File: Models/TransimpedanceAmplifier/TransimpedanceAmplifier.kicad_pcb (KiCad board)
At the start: 2 copper layers, 107 parts, among them J1 Conn_01x02_Socket, J10 Conn_01x02_Pin, J11 Conn_01x24_Socket, J14 Conn_01x24_Socket, J2 Conn_01x02_Socket, J3 Conn_01x03_Pin, J4 Conn_01x02_Pin, J5 Conn_01x02_Pin, J6 Conn_01x02_Pin, J7 Conn_01x02_Pin, J8 Conn_01x02_Pin, J9 Conn_01x02_Pin, Q1 Q_PNP, Q2 Q_NPN, U1 LM7905, -5V, 5%, U10 DAC81401, U11 ISO7641FM, U12 ISO7641FM, U13 ADS8699, U2 LM7805, 5V, 5%, U3 OPA828, U4 AD8615, U5 OP37GPZ, U6 LM7915, -15V, 5%, U7 LM7815, 15V, 5%, U8 LM7805, 5V, 5%, U9 TLV76133, 3.3V, 1%

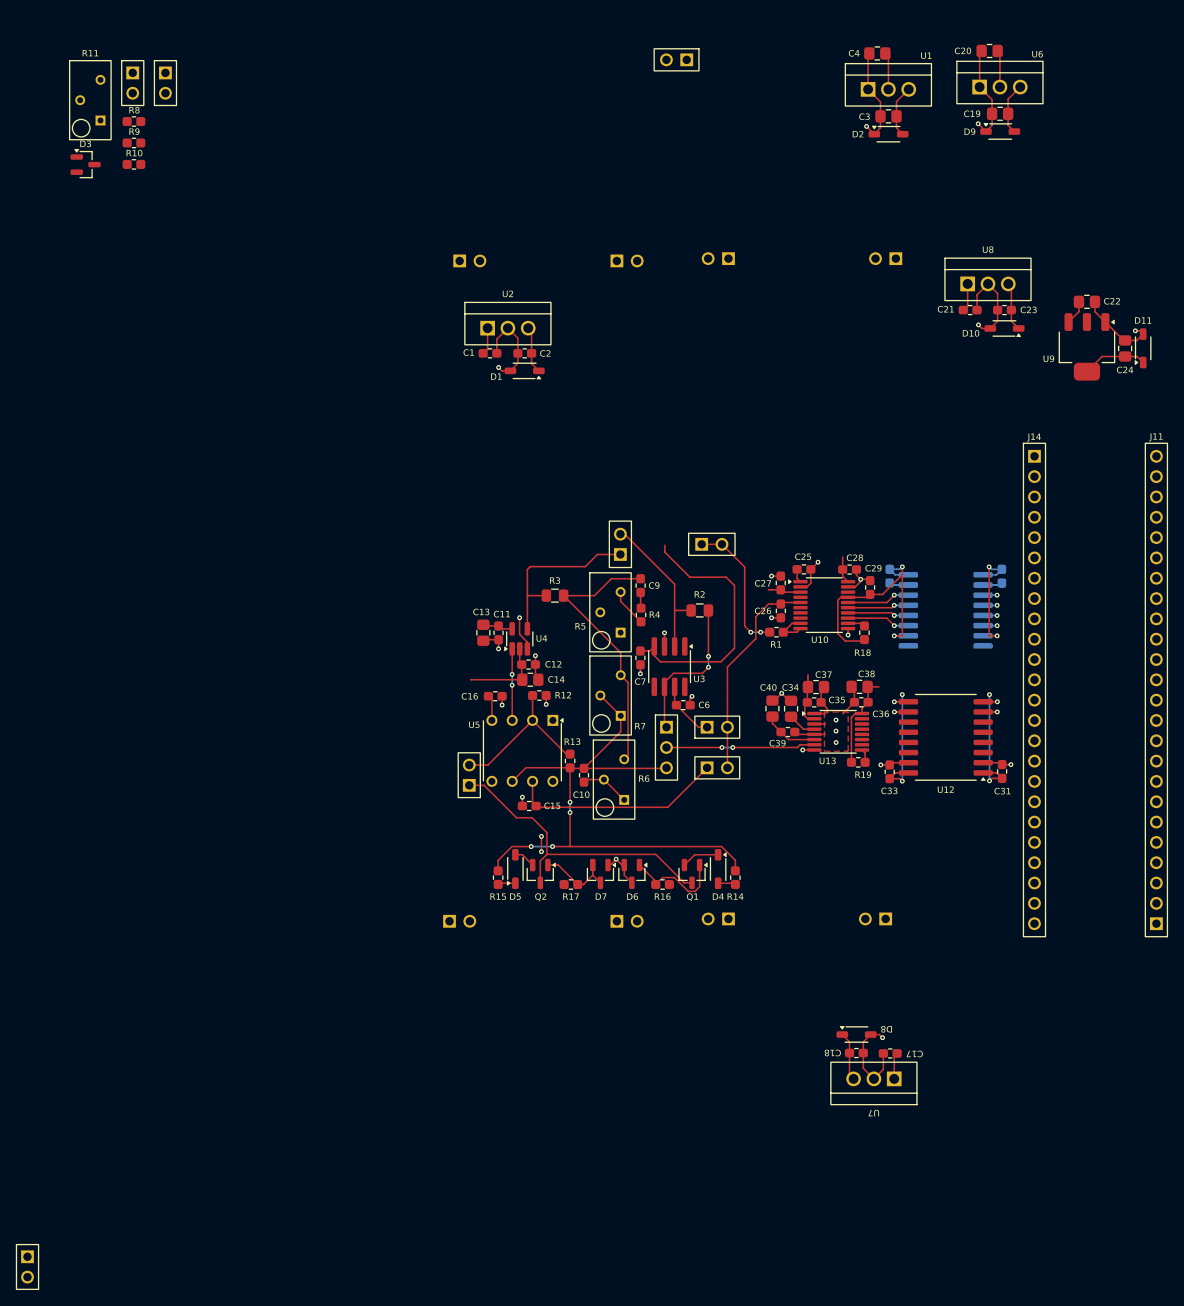
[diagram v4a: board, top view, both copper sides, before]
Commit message: Finalized the positions of all expensive chips and their nearby components
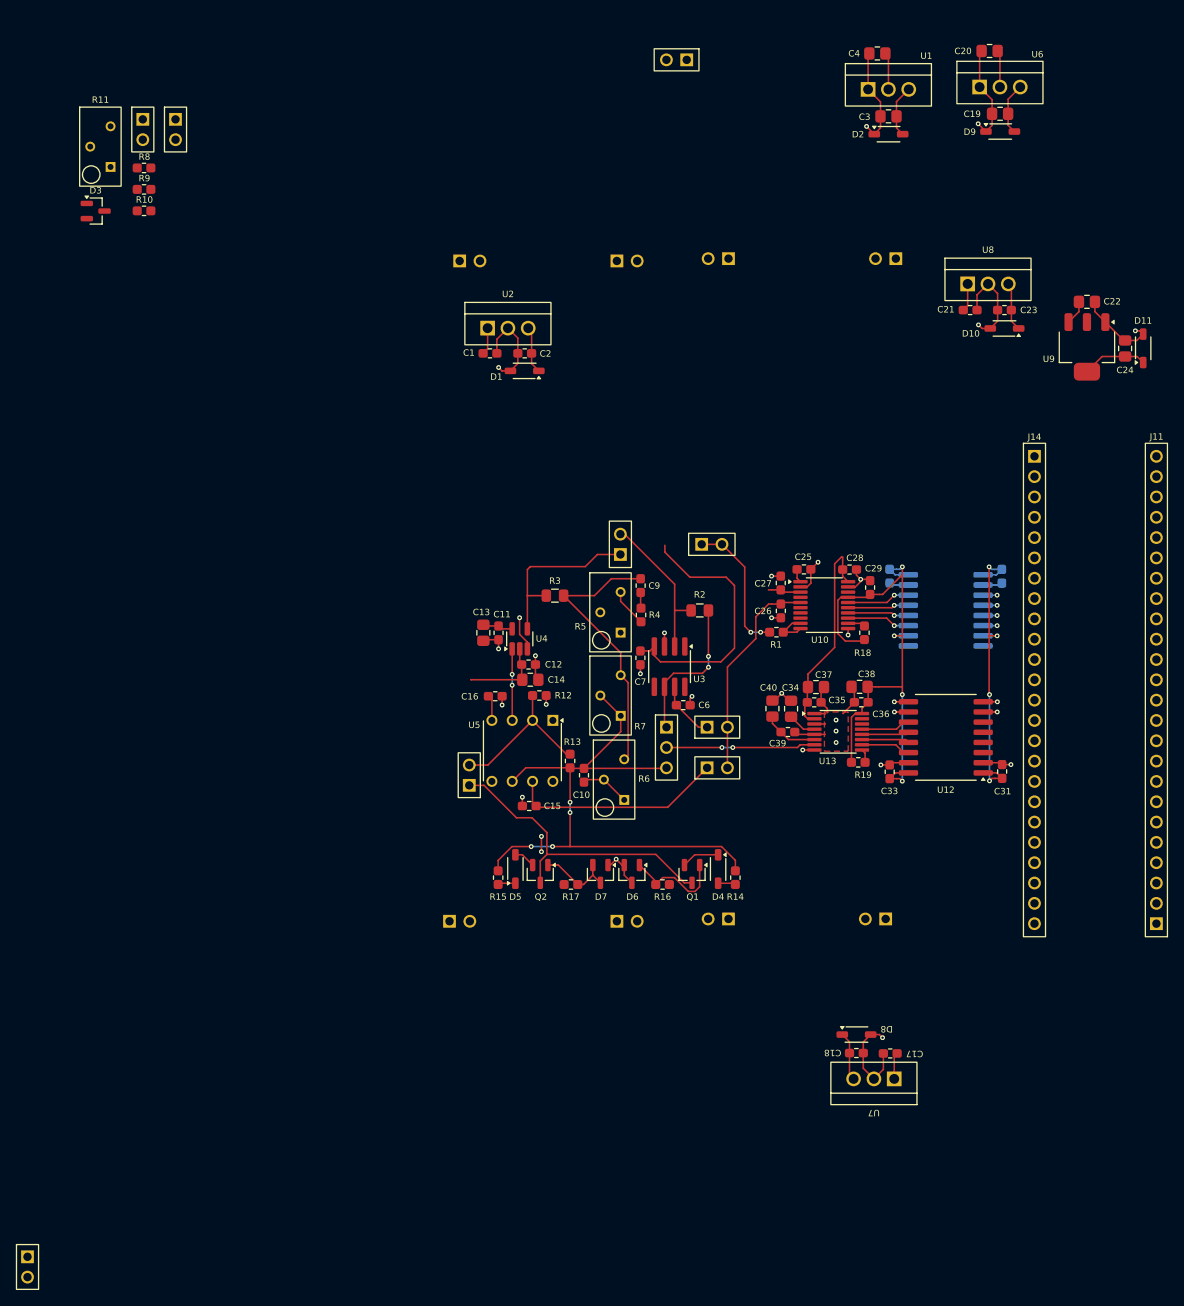
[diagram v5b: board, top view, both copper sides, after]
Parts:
- moved J6 5.94 mm to (37.8, 33.8)
- moved J7 5.94 mm to (41.9, 33.8)
- moved R11 5.94 mm to (32.5, 36.0)
- moved D3 5.94 mm to (31.9, 44.0)
- moved R10 5.94 mm to (38.0, 44.0)
- moved R8 5.94 mm to (38.0, 38.6)
- moved R9 5.94 mm to (38.0, 41.3)
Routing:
- net /5V_Converter: track 9.17 -> 25.8 mm
- net /3.3V_Converter: track 37.5 -> 47.7 mm
- net /CPU/Isolation/3.3V_Digital: track 25.8 -> 33.1 mm
- net /CPU/ADC/MOSI: track 0.00 -> 6.21 mm
- net /CPU/ADC/MISO: track 0.00 -> 6.17 mm
- net /CPU/ADC/CS: track 0.00 -> 5.95 mm
- net /CPU/ADC/SCK: track 0.00 -> 5.92 mm
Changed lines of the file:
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@@
 	(footprint "Connector_Custom:PinHeader_1x2"
 		(layer "F.Cu")
-		(at 40.6325 28.005)
+		(at 41.89 33.81)
 		(property "Reference" "J7"
 			(at 0.0025 -3.5625 0)
@@
 	)
 	(footprint "TwoTerminal:RESC0603"
+		(locked yes)
 		(layer "F.Cu")
 		(at 117.005 96.645 180)
@@
 	)
 	(footprint "TwoTerminal:CAPC0603"
+		(locked yes)
 		(layer "F.Cu")
 		(at 121.7275 105.415)
@@
 	(footprint "Connector_Custom:PinHeader_1x2"
 		(layer "F.Cu")
-		(at 36.5425 28.005)
+		(at 37.8 33.81)
 		(property "Reference" "J6"
 			(at 0.0025 -3.5625 0)
@@
 	)
 	(footprint "TwoTerminal:CAPC0805"
+		(locked yes)
 		(layer "F.Cu")
 		(at 127.3975 103.475 180)
@@
 	)
 	(footprint "IC:DAC81401"
+		(locked yes)
 		(layer "F.Cu")
 		(at 122.9875 93.26)
@@
 	)
 	(footprint "TwoTerminal:CAPC0805"
+		(locked yes)
 		(layer "F.Cu")
 		(at 116.505 106.19429 90)
@@
 	)
 	(footprint "IC:ISO7641FM"
+		(locked yes)
 		(layer "F.Cu")
 		(at 138.18 109.79 180)
@@
 	)
 	(footprint "TwoTerminal:RESC0603"
+		(locked yes)
 		(layer "F.Cu")
 		(at 127.235 112.91429 180)
@@
 	(footprint "ThreeTerminal:SOT-23"
 		(layer "F.Cu")
-		(at 30.6525 38.195)
+		(at 31.91 44)
 		(property "Reference" "D3"
 			(at -0.005 -2.5625 0)
@@
 	)
 	(footprint "TwoTerminal:CAPC0603"
+		(locked yes)
 		(layer "F.Cu")
 		(at 127.6075 105.405 180)
@@
 	)
 	(footprint "TwoTerminal:RESC0603"
+		(locked yes)
 		(layer "F.Cu")
 		(at 128.005 96.715 -90)
@@
 	)
 	(footprint "TwoTerminal:CAPC0603"
+		(locked yes)
 		(layer "F.Cu")
 		(at 126.145 88.81179)
@@
 	)
 	(footprint "TwoTerminal:CAPC0805"
+		(locked yes)
 		(layer "F.Cu")
 		(at 118.835 106.21429 90)
@@
 	)
 	(footprint "TwoTerminal:CAPC0603"
+		(locked yes)
 		(layer "F.Cu")
 		(at 131.16 114.095 90)
@@
 	(footprint "TwoTerminal:RESC0603"
 		(layer "F.Cu")
-		(at 36.6975 32.81)
+		(at 37.955 38.615)
 		(property "Reference" "R8"
 			(at 0.0475 -1.385 0)
@@
 	)
 	(footprint "IC:ADS8699"
+		(locked yes)
 		(layer "F.Cu")
 		(at 124.725 109.09429)
@@
 	)
 	(footprint "TwoTerminal:CAPC0603"
+		(locked yes)
 		(layer "F.Cu")
 		(at 117.545 90.495 90)
@@
 	(footprint "ThreeTerminal:Bourns_3296Y"
 		(layer "F.Cu")
-		(at 31.2425 30.145)
+		(at 32.5 35.95)
 		(property "Reference" "R11"
 			(at 0.0075 -5.85 0)
@@
 	)
 	(footprint "TwoTerminal:CAPC0603"
+		(locked yes)
 		(layer "F.Cu")
 		(at 117.555 93.985 -90)
@@
 	)
 	(footprint "TwoTerminal:CAPC0603"
+		(locked yes)
 		(layer "F.Cu")
 		(at 120.445 88.795)
@@
 	(footprint "TwoTerminal:RESC0603"
 		(layer "F.Cu")
-		(at 36.6975 38.17)
+		(at 37.955 43.975)
 		(property "Reference" "R10"
 			(at 0.0475 -1.385 0)
@@
 	(footprint "TwoTerminal:RESC0603"
 		(layer "F.Cu")
-		(at 36.6975 35.49)
+		(at 37.955 41.295)
 		(property "Reference" "R9"
 			(at 0.0475 -1.385 0)
@@
 	)
 	(footprint "TwoTerminal:CAPC0603"
+		(locked yes)
 		(layer "F.Cu")
 		(at 145.22 114.055 90)
@@
 	)
 	(footprint "TwoTerminal:CAPC0805"
+		(locked yes)
 		(layer "F.Cu")
 		(at 121.9475 103.505)
@@
 	)
 	(footprint "TwoTerminal:CAPC0603"
+		(locked yes)
 		(layer "F.Cu")
 		(at 128.715 91.06179 90)
@@
 	)
 	(footprint "TwoTerminal:CAPC0603"
+		(locked yes)
 		(layer "F.Cu")
 		(at 118.435 109.12429)
@@
 	)
 	(footprint "IC:ISO7641FM"
+		(locked yes)
 		(layer "B.Cu")
 		(at 138.1625 93.92 180)
@@
 	)
 	(footprint "TwoTerminal:CAPC0603"
+		(locked yes)
 		(layer "B.Cu")
 		(at 145.1825 89.65 -90)
@@
 	)
 	(footprint "TwoTerminal:CAPC0603"
+		(locked yes)
 		(layer "B.Cu")
 		(at 131.1525 89.64 -90)
@@
 	)
 	(segment
+		(start 120.9475 101.8825)
+		(end 124.284 98.546)
+		(width 0.2)
+		(layer "F.Cu")
+		(net 24)
+	)
+	(segment
 		(start 146.37 56.38)
 		(end 146.37 57.7625)
@@
 	)
 	(segment
+		(start 124.284 98.546)
+		(end 124.284 88.09569)
+		(width 0.2)
+		(layer "F.Cu")
+		(net 24)
+	)
+	(segment
+		(start 120.9475 101.975)
+		(end 120.9475 101.8825)
+		(width 0.2)
+		(layer "F.Cu")
+		(net 24)
+	)
+	(segment
+		(start 124.284 88.09569)
+		(end 125.1179 87.26179)
+		(width 0.2)
+		(layer "F.Cu")
+		(net 24)
+	)
+	(segment
+		(start 125.1179 87.26179)
+		(end 125.285 87.26179)
+		(width 0.2)
+		(layer "F.Cu")
+		(net 24)
+	)
+	(segment
 		(start 146.37 53.49)
 		(end 145.99 53.11)
@@
 	)
 	(segment
+		(start 129.8075 103.475)
+		(end 132.7375 103.475)
+		(width 0.2)
+		(layer "F.Cu")
+		(net 25)
+	)
+	(segment
 		(start 160.59 62.1825)
 		(end 162.095 62.1825)
@@
 	)
 	(segment
+		(start 132.7375 103.475)
+		(end 132.7425 103.47)
+		(width 0.2)
+		(layer "F.Cu")
+		(net 25)
+	)
+	(segment
 		(start 157.7175 62.1825)
 		(end 155.82 64.08)
@@
 	)
 	(segment
+		(start 132.7425 104.4425)
+		(end 132.74 104.445)
+		(width 0.2)
+		(layer "F.Cu")
+		(net 25)
+	)
+	(segment
 		(start 132.7425 88.48)
 		(end 132.7425 89.45)
@@
 	)
 	(segment
+		(start 132.7425 97.1)
+		(end 132.7425 103.47)
+		(width 0.2)
+		(layer "F.Cu")
+		(net 25)
+	)
+	(segment
+		(start 132.7425 103.47)
+		(end 132.7425 104.4425)
+		(width 0.2)
+		(layer "F.Cu")
+		(net 25)
+	)
+	(segment
 		(start 132.7425 89.45)
 		(end 132.7425 97.1)
@@
 	)
 	(segment
+		(start 143.5925 97.1)
+		(end 143.5925 104.3975)
+		(width 0.2)
+		(layer "F.Cu")
+		(net 71)
+	)
+	(segment
 		(start 143.5925 88.48)
 		(end 143.5925 97.1)
@@
 	)
 	(segment
+		(start 143.5925 104.3975)
+		(end 143.64 104.445)
+		(width 0.2)
+		(layer "F.Cu")
+		(net 71)
+	)
+	(segment
 		(start 142.85 106.615)
 		(end 144.61 106.615)
@@
 		(net 121)
 	)
+	(segment
+		(start 133.24571 109.41929)
+		(end 133.51 109.155)
+		(width 0.2)
+		(layer "F.Cu")
+		(net 122)
+	)
+	(segment
+		(start 127.7025 109.41929)
+		(end 133.24571 109.41929)
+		(width 0.2)
+		(layer "F.Cu")
+		(net 122)
+	)
+	(segment
+		(start 133.51 110.425)
+		(end 133.15429 110.06929)
+		(width 0.2)
+		(layer "F.Cu")
+		(net 123)
+	)
+	(segment
+		(start 133.15429 110.06929)
+		(end 127.7025 110.06929)
+		(width 0.2)
+		(layer "F.Cu")
+		(net 123)
+	)
+	(segment
+		(start 127.7025 108.76929)
+		(end 132.011302 108.76929)
+		(width 0.2)
+		(layer "F.Cu")
+		(net 124)
+	)
+	(segment
+		(start 132.011302 108.76929)
+		(end 132.895592 107.885)
+		(width 0.2)
+		(layer "F.Cu")
+		(net 124)
+	)
+	(segment
+		(start 132.895592 107.885)
+		(end 133.51 107.885)
+		(width 0.2)
+		(layer "F.Cu")
+		(net 124)
+	)
+	(segment
+		(start 132.895592 111.695)
+		(end 133.51 111.695)
+		(width 0.2)
+		(layer "F.Cu")
+		(net 125)
+	)
+	(segment
+		(start 131.919882 110.71929)
+		(end 132.895592 111.695)
+		(width 0.2)
+		(layer "F.Cu")
+		(net 125)
+	)
+	(segment
+		(start 127.7025 110.71929)
+		(end 131.919882 110.71929)
+		(width 0.2)
+		(layer "F.Cu")
+		(net 125)
+	)
 	(zone

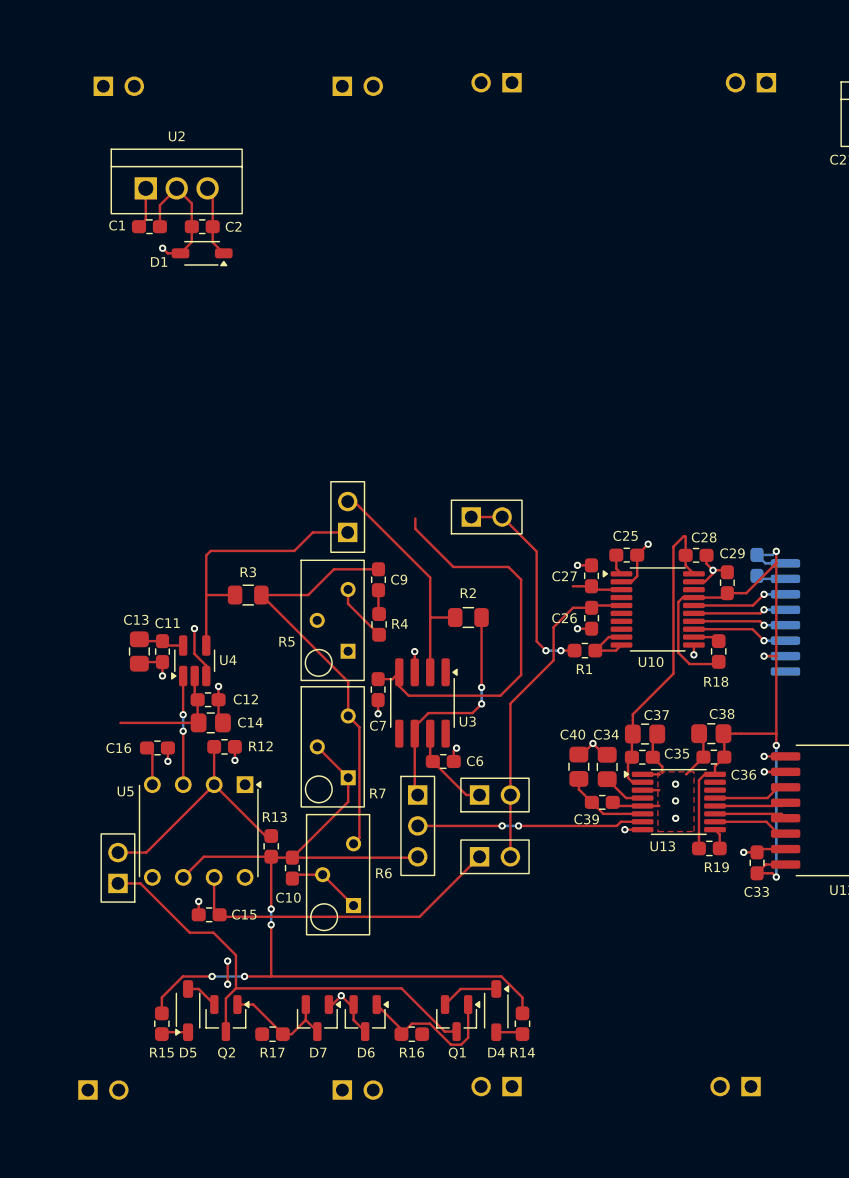
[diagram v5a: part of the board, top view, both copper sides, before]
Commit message: Positions of the battery modules are now locked
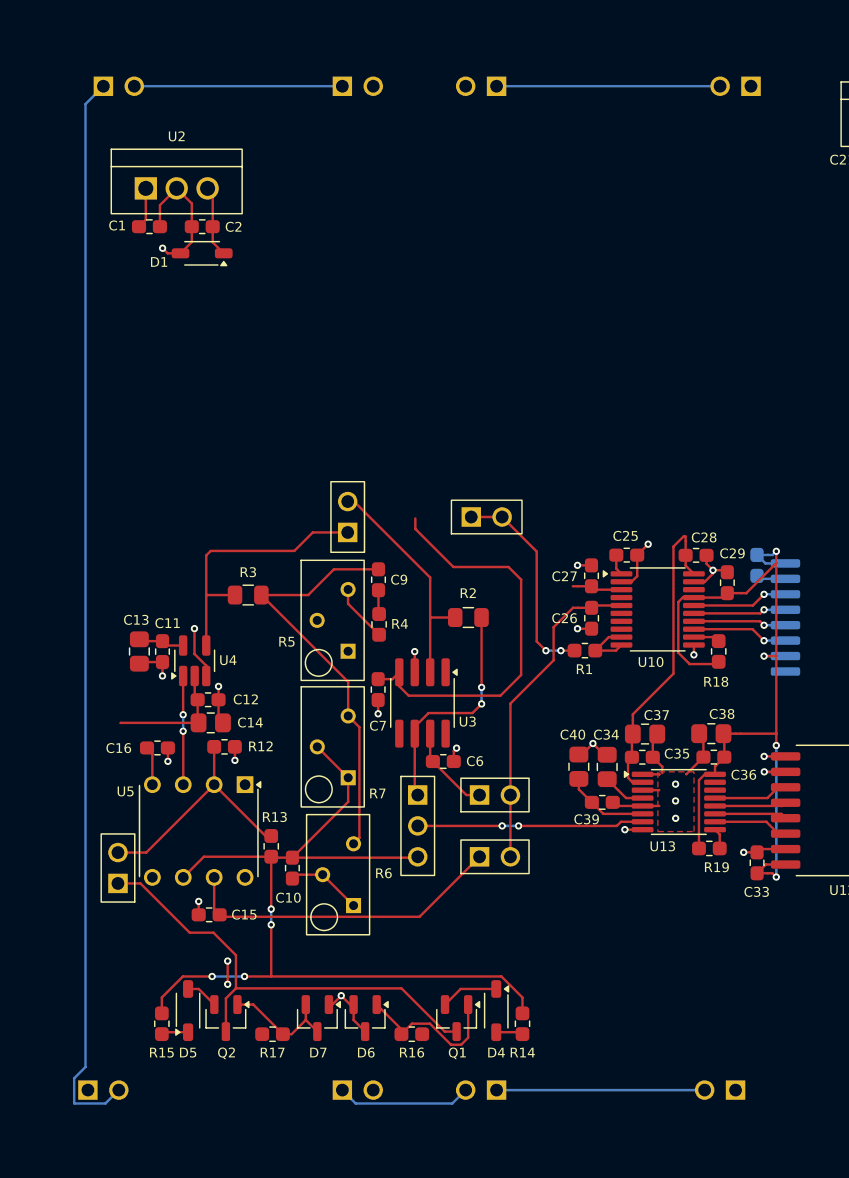
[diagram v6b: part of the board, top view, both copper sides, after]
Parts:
- moved BT1 1.30 mm to (118.9, 91.5)
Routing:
- net Net-(BT2-BT1(+)): track 0.00 -> 88.7 mm
- net Net-(BT1-BT3(-)): track 0.00 -> 18.4 mm
- net Net-(BT2-BT1(-)): track 0.00 -> 17.1 mm
- net Net-(BT1-BT1(-)): track 0.00 -> 17.1 mm
- net Net-(BT1-BT2(-)): track 0.00 -> 11.1 mm
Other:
- board text removed: "27 V"
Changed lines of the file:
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@@
 	)
 	(footprint "Connector_Custom:BatteryModule"
+		(locked yes)
 		(layer "B.Cu")
 		(at 87.87 91.51 -90)
@@
 			(unlocked yes)
 			(layer "B.SilkS")
+			(hide yes)
 			(effects
 				(font
@@
 	)
 	(footprint "Connector_Custom:BatteryModule"
+		(locked yes)
 		(layer "B.Cu")
-		(at 120.2 91.22 90)
+		(at 118.93 91.51 90)
 		(property "Reference" "BT1"
 			(at 0.0225 14.7625 270)
 			(unlocked yes)
 			(layer "B.SilkS")
+			(hide yes)
 			(effects
 				(font
@@
 			(polygon
 				(pts
-					(xy 115.715 63.835) (xy 111.985 63.835) (xy 111.985 60.105) (xy 115.715 60.105)
+					(xy 114.445 64.125) (xy 110.715 64.125) (xy 110.715 60.395) (xy 114.445 60.395)
 				)
 			)
@@
 			(polygon
 				(pts
-					(xy 115.715 83.335) (xy 111.985 83.335) (xy 111.985 79.605) (xy 115.715 79.605)
+					(xy 114.445 83.625) (xy 110.715 83.625) (xy 110.715 79.895) (xy 114.445 79.895)
 				)
 			)
@@
 			(polygon
 				(pts
-					(xy 115.715 102.835) (xy 111.985 102.835) (xy 111.985 99.105) (xy 115.715 99.105)
+					(xy 114.445 103.125) (xy 110.715 103.125) (xy 110.715 99.395) (xy 114.445 99.395)
 				)
 			)
@@
 			(polygon
 				(pts
-					(xy 115.715 122.335) (xy 111.985 122.335) (xy 111.985 118.605) (xy 115.715 118.605)
+					(xy 114.445 122.625) (xy 110.715 122.625) (xy 110.715 118.895) (xy 114.445 118.895)
 				)
 			)
@@
 			(polygon
 				(pts
-					(xy 128.415 63.835) (xy 124.685 63.835) (xy 124.685 60.105) (xy 128.415 60.105)
+					(xy 127.145 64.125) (xy 123.415 64.125) (xy 123.415 60.395) (xy 127.145 60.395)
 				)
 			)
@@
 			(polygon
 				(pts
-					(xy 128.415 83.335) (xy 124.685 83.335) (xy 124.685 79.605) (xy 128.415 79.605)
+					(xy 127.145 83.625) (xy 123.415 83.625) (xy 123.415 79.895) (xy 127.145 79.895)
 				)
 			)
@@
 			(polygon
 				(pts
-					(xy 128.415 102.835) (xy 124.685 102.835) (xy 124.685 99.105) (xy 128.415 99.105)
+					(xy 127.145 103.125) (xy 123.415 103.125) (xy 123.415 99.395) (xy 127.145 99.395)
 				)
 			)
@@
 			(polygon
 				(pts
-					(xy 128.415 122.335) (xy 124.685 122.335) (xy 124.685 118.605) (xy 128.415 118.605)
+					(xy 127.145 122.625) (xy 123.415 122.625) (xy 123.415 118.895) (xy 127.145 118.895)
 				)
 			)
@@
 	)
 	(gr_rect
-		(start 141.36 73.57)
-		(end 166.16 136.57)
+		(start 73.94 48.19)
+		(end 134.76 134.83)
 		(stroke
 			(width 0.1)
@@
 	)
 	(gr_rect
-		(start 73.3 47.26)
-		(end 135.11 136.46)
-		(stroke
-			(width 0.1)
-			(type default)
-		)
-		(fill no)
-		(layer "Dwgs.User")
-	)
-	(gr_rect
-		(start 135.11 47.26)
-		(end 166.24 67.21)
+		(start 134.75 48.19)
+		(end 166.24 66.22)
 		(stroke
 			(width 0.1)
@@
 		)
 	)
-	(gr_text "27 V"
-		(at 129.42 130.02 0)
-		(layer "User.2")
-		(effects
-			(font
-				(size 0.8 0.8)
-				(thickness 0.12)
-			)
-			(justify left bottom)
-		)
-	)
 	(gr_text "3.3 V"
 		(at 148.64 65.14 0)
@@
 	)
 	(segment
+		(start 109.74 132.78)
+		(end 126.85 132.78)
+		(width 0.2)
+		(layer "B.Cu")
+		(net 1)
+	)
+	(segment
+		(start 109.74 50.24)
+		(end 128.12 50.24)
+		(width 0.2)
+		(layer "B.Cu")
+		(net 2)
+	)
+	(segment
 		(start 140.91 53.11)
 		(end 140.91 55.83)
@@
 	)
 	(segment
+		(start 106.099 133.881)
+		(end 98.161 133.881)
+		(width 0.2)
+		(layer "B.Cu")
+		(net 6)
+	)
+	(segment
+		(start 107.2 132.78)
+		(end 106.099 133.881)
+		(width 0.2)
+		(layer "B.Cu")
+		(net 6)
+	)
+	(segment
+		(start 98.161 133.881)
+		(end 97.06 132.78)
+		(width 0.2)
+		(layer "B.Cu")
+		(net 6)
+	)
+	(segment
 		(start 144.9425 24.28125)
 		(end 144.655 23.99375)
@@
 	)
 	(segment
+		(start 75.01 131.81)
+		(end 75.01 133.852)
+		(width 0.2)
+		(layer "B.Cu")
+		(net 8)
+	)
+	(segment
+		(start 75.94 130.88)
+		(end 75.01 131.81)
+		(width 0.2)
+		(layer "B.Cu")
+		(net 8)
+	)
+	(segment
+		(start 75.01 133.852)
+		(end 75.039 133.881)
+		(width 0.2)
+		(layer "B.Cu")
+		(net 8)
+	)
+	(segment
+		(start 75.039 133.881)
+		(end 77.579 133.881)
+		(width 0.2)
+		(layer "B.Cu")
+		(net 8)
+	)
+	(segment
+		(start 75.94 51.71)
+		(end 75.94 130.88)
+		(width 0.2)
+		(layer "B.Cu")
+		(net 8)
+	)
+	(segment
+		(start 77.579 133.881)
+		(end 78.68 132.78)
+		(width 0.2)
+		(layer "B.Cu")
+		(net 8)
+	)
+	(segment
+		(start 77.41 50.24)
+		(end 75.94 51.71)
+		(width 0.2)
+		(layer "B.Cu")
+		(net 8)
+	)
+	(segment
+		(start 79.95 50.24)
+		(end 97.06 50.24)
+		(width 0.2)
+		(layer "B.Cu")
+		(net 9)
+	)
+	(segment
